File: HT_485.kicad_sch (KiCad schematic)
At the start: 80 parts, among them J1 POWER, J2 485, J3 PT1000, J4 H/T Sensor, J5 PRG, Q1 BC817, Q2 BC817, Q3 BC817, Q4 BC817, U1 MAX14786EAUD+T, U2 TL082, U3 LM2576D2TR4-3.3G, U4 ESP32-S3-WROOM-1-N16R8, U6 L7815

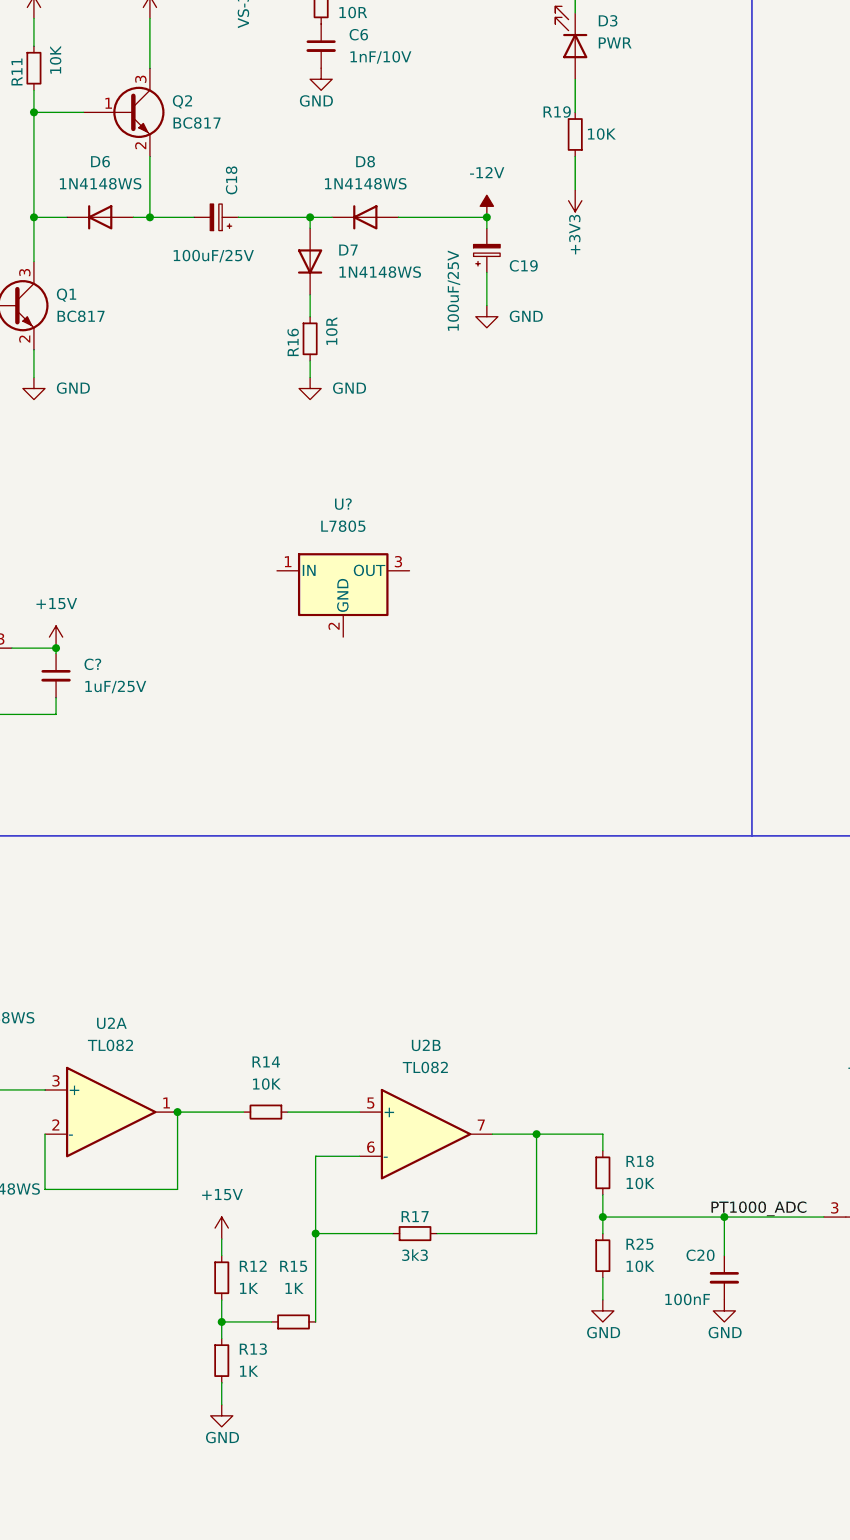
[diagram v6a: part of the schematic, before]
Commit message: Sistemate resistenze di centratura PT1000
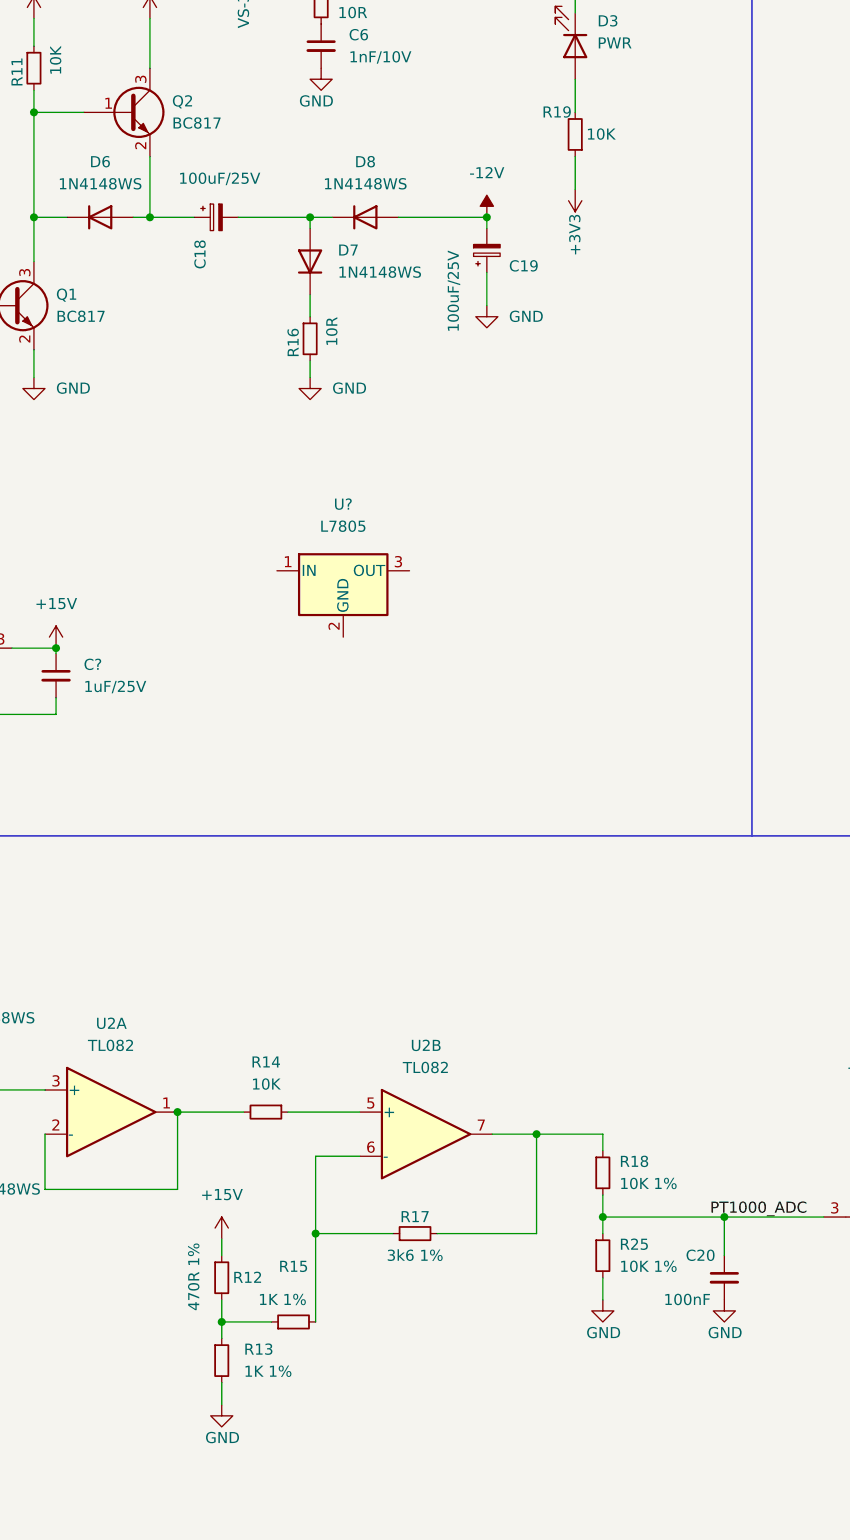
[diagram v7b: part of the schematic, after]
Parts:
- R12: value 1K -> 470R 1%
- R13, R15: value 1K -> 1K 1%
- R17: value 3k3 -> 3k6 1%
- R18, R25: value 10K -> 10K 1%
- U?: footprint (none) -> Package_TO_SOT_SMD:TO-263-2
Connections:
- net at D7.2 (A), D8.1 (K): now also C18.2; no longer C18.1
- net at D6.2 (A), Q2.2 (E): now also C18.1; no longer C18.2
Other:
- moved on the sheet: C18
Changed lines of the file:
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@@
     (in_bom yes) (on_board yes)
     (property "Reference" "R17" (id 0) (at 109.855 201.295 90))
-    (property "Value" "3k3" (id 1) (at 109.855 205.74 90))
+    (property "Value" "3k6 1%" (id 1) (at 109.855 205.74 90))
     (property "Footprint" "Resistor_SMD:R_0805_2012Metric_Pad1.20x1.40mm_HandSolder" (id 2) (at 109.855 203.2 0)
       (effects (font (size 1.27 1.27)) hide)
@@
   )
   (symbol (lib_id "Device:R_Small") (at 87.63 208.28 0) (unit 1)
-    (in_bom yes) (on_board yes) (fields_autoplaced)
-    (property "Reference" "R12" (id 0) (at 89.535 207.0099 0)
-      (effects (font (size 1.27 1.27)) (justify left))
-    )
-    (property "Value" "1K" (id 1) (at 89.535 209.5499 0)
+    (in_bom yes) (on_board yes)
+    (property "Reference" "R12" (id 0) (at 88.9 208.28 0)
+      (effects (font (size 1.27 1.27)) (justify left))
+    )
+    (property "Value" "470R 1%" (id 1) (at 84.455 212.09 90)
       (effects (font (size 1.27 1.27)) (justify left))
     )
@@
     (pin "2")
   )
-  (symbol (lib_id "Device:C_Polarized_Small") (at 86.995 86.36 270) (mirror x) (unit 1)
-    (in_bom yes) (on_board yes)
-    (property "Reference" "C18" (id 0) (at 88.8112 83.82 0)
-      (effects (font (size 1.27 1.27)) (justify left))
-    )
-    (property "Value" "100uF/25V" (id 1) (at 81.915 90.805 90)
+  (symbol (lib_id "Device:C_Polarized_Small") (at 86.995 86.36 90) (mirror x) (unit 1)
+    (in_bom yes) (on_board yes)
+    (property "Reference" "C18" (id 0) (at 85.1788 88.9 0)
+      (effects (font (size 1.27 1.27)) (justify left))
+    )
+    (property "Value" "100uF/25V" (id 1) (at 92.075 81.915 90)
       (effects (font (size 1.27 1.27)) (justify left))
     )
@@
   (symbol (lib_id "Device:R_Small") (at 131.445 196.215 0) (unit 1)
     (in_bom yes) (on_board yes) (fields_autoplaced)
-    (property "Reference" "R18" (id 0) (at 133.985 194.9449 0)
-      (effects (font (size 1.27 1.27)) (justify left))
-    )
-    (property "Value" "10K" (id 1) (at 133.985 197.4849 0)
+    (property "Reference" "R18" (id 0) (at 133.35 194.9449 0)
+      (effects (font (size 1.27 1.27)) (justify left))
+    )
+    (property "Value" "10K 1%" (id 1) (at 133.35 197.4849 0)
       (effects (font (size 1.27 1.27)) (justify left))
     )
@@
     (property "Reference" "U?" (id 0) (at 101.6 119.38 0))
     (property "Value" "L7805" (id 1) (at 101.6 121.92 0))
-    (property "Footprint" "" (id 2) (at 102.235 130.81 0)
+    (property "Footprint" "Package_TO_SOT_SMD:TO-263-2" (id 2) (at 102.235 130.81 0)
       (effects (font (size 1.27 1.27) italic) (justify left) hide)
     )
@@
   (symbol (lib_id "Device:R_Small") (at 87.63 217.805 0) (unit 1)
     (in_bom yes) (on_board yes) (fields_autoplaced)
-    (property "Reference" "R13" (id 0) (at 89.535 216.5349 0)
-      (effects (font (size 1.27 1.27)) (justify left))
-    )
-    (property "Value" "1K" (id 1) (at 89.535 219.0749 0)
+    (property "Reference" "R13" (id 0) (at 90.17 216.5349 0)
+      (effects (font (size 1.27 1.27)) (justify left))
+    )
+    (property "Value" "1K 1%" (id 1) (at 90.17 219.0749 0)
       (effects (font (size 1.27 1.27)) (justify left))
     )
@@
   )
   (symbol (lib_id "Device:R_Small") (at 95.885 213.36 90) (unit 1)
-    (in_bom yes) (on_board yes) (fields_autoplaced)
+    (in_bom yes) (on_board yes)
     (property "Reference" "R15" (id 0) (at 95.885 207.01 90))
-    (property "Value" "1K" (id 1) (at 95.885 209.55 90))
+    (property "Value" "1K 1%" (id 1) (at 94.615 210.82 90))
     (property "Footprint" "Resistor_SMD:R_0805_2012Metric_Pad1.20x1.40mm_HandSolder" (id 2) (at 95.885 213.36 0)
       (effects (font (size 1.27 1.27)) hide)
@@
   (symbol (lib_id "Device:R_Small") (at 131.445 205.74 0) (unit 1)
     (in_bom yes) (on_board yes) (fields_autoplaced)
-    (property "Reference" "R25" (id 0) (at 133.985 204.4699 0)
-      (effects (font (size 1.27 1.27)) (justify left))
-    )
-    (property "Value" "10K" (id 1) (at 133.985 207.0099 0)
+    (property "Reference" "R25" (id 0) (at 133.35 204.4699 0)
+      (effects (font (size 1.27 1.27)) (justify left))
+    )
+    (property "Value" "10K 1%" (id 1) (at 133.35 207.0099 0)
       (effects (font (size 1.27 1.27)) (justify left))
     )
@@
     )
     (path "/37a4da1b-b23e-4c99-92c5-1edd1e260509"
-      (reference "R12") (unit 1) (value "1K") (footprint "Resistor_SMD:R_0805_2012Metric_Pad1.20x1.40mm_HandSolder")
+      (reference "R12") (unit 1) (value "470R 1%") (footprint "Resistor_SMD:R_0805_2012Metric_Pad1.20x1.40mm_HandSolder")
     )
     (path "/9b2c5abb-3c78-49d8-8ccb-d7a77fc4039f"
-      (reference "R13") (unit 1) (value "1K") (footprint "Resistor_SMD:R_0805_2012Metric_Pad1.20x1.40mm_HandSolder")
+      (reference "R13") (unit 1) (value "1K 1%") (footprint "Resistor_SMD:R_0805_2012Metric_Pad1.20x1.40mm_HandSolder")
     )
     (path "/c2ad6d7a-43e9-4769-ab7d-5b48aedd331e"
@@
     )
     (path "/dafc20e6-5160-4991-b11c-f4df07558de3"
-      (reference "R15") (unit 1) (value "1K") (footprint "Resistor_SMD:R_0805_2012Metric_Pad1.20x1.40mm_HandSolder")
+      (reference "R15") (unit 1) (value "1K 1%") (footprint "Resistor_SMD:R_0805_2012Metric_Pad1.20x1.40mm_HandSolder")
     )
     (path "/c722abe2-39f6-4182-8f35-73ac3a447bdd"
@@
     )
     (path "/2ea8c421-e022-4b53-ab9d-747574ed23fe"
-      (reference "R17") (unit 1) (value "3k3") (footprint "Resistor_SMD:R_0805_2012Metric_Pad1.20x1.40mm_HandSolder")
+      (reference "R17") (unit 1) (value "3k6 1%") (footprint "Resistor_SMD:R_0805_2012Metric_Pad1.20x1.40mm_HandSolder")
     )
     (path "/7ce32af9-e8f8-4200-8b4f-d83e817f1fc3"
-      (reference "R18") (unit 1) (value "10K") (footprint "Resistor_SMD:R_0805_2012Metric_Pad1.20x1.40mm_HandSolder")
+      (reference "R18") (unit 1) (value "10K 1%") (footprint "Resistor_SMD:R_0805_2012Metric_Pad1.20x1.40mm_HandSolder")
     )
     (path "/a570d174-ff6a-411e-b642-a015e64749d6"
@@
     )
     (path "/ff6f4ff7-c949-4b19-91be-7f03370d9dc7"
-      (reference "R25") (unit 1) (value "10K") (footprint "Resistor_SMD:R_0805_2012Metric_Pad1.20x1.40mm_HandSolder")
+      (reference "R25") (unit 1) (value "10K 1%") (footprint "Resistor_SMD:R_0805_2012Metric_Pad1.20x1.40mm_HandSolder")
     )
     (path "/e59741c1-43ad-443b-8cb7-ceec55dffecf"

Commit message: Aggiunto progetto Sensore i2C
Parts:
- R12: value 470R 1% -> 430R 1%
- R17: value 3k6 1% -> 3K3 1%
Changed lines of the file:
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@@
     (in_bom yes) (on_board yes)
     (property "Reference" "R17" (id 0) (at 109.855 201.295 90))
-    (property "Value" "3k6 1%" (id 1) (at 109.855 205.74 90))
+    (property "Value" "3K3 1%" (id 1) (at 109.855 205.74 90))
     (property "Footprint" "Resistor_SMD:R_0805_2012Metric_Pad1.20x1.40mm_HandSolder" (id 2) (at 109.855 203.2 0)
       (effects (font (size 1.27 1.27)) hide)
@@
       (effects (font (size 1.27 1.27)) (justify left))
     )
-    (property "Value" "470R 1%" (id 1) (at 84.455 212.09 90)
+    (property "Value" "430R 1%" (id 1) (at 84.455 212.09 90)
       (effects (font (size 1.27 1.27)) (justify left))
     )
@@
     )
     (path "/37a4da1b-b23e-4c99-92c5-1edd1e260509"
-      (reference "R12") (unit 1) (value "470R 1%") (footprint "Resistor_SMD:R_0805_2012Metric_Pad1.20x1.40mm_HandSolder")
+      (reference "R12") (unit 1) (value "430R 1%") (footprint "Resistor_SMD:R_0805_2012Metric_Pad1.20x1.40mm_HandSolder")
     )
     (path "/9b2c5abb-3c78-49d8-8ccb-d7a77fc4039f"
@@
     )
     (path "/2ea8c421-e022-4b53-ab9d-747574ed23fe"
-      (reference "R17") (unit 1) (value "3k6 1%") (footprint "Resistor_SMD:R_0805_2012Metric_Pad1.20x1.40mm_HandSolder")
+      (reference "R17") (unit 1) (value "3K3 1%") (footprint "Resistor_SMD:R_0805_2012Metric_Pad1.20x1.40mm_HandSolder")
     )
     (path "/7ce32af9-e8f8-4200-8b4f-d83e817f1fc3"
